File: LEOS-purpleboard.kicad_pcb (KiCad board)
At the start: 2 copper layers, 100 x 76.5 mm, 5 parts, among them J3 Conn_01x07_Socket, J4 Conn_01x07_Socket, J5 Conn_01x06_Socket, J6 Conn_01x06_Socket, J7 Conn_01x04_Pin

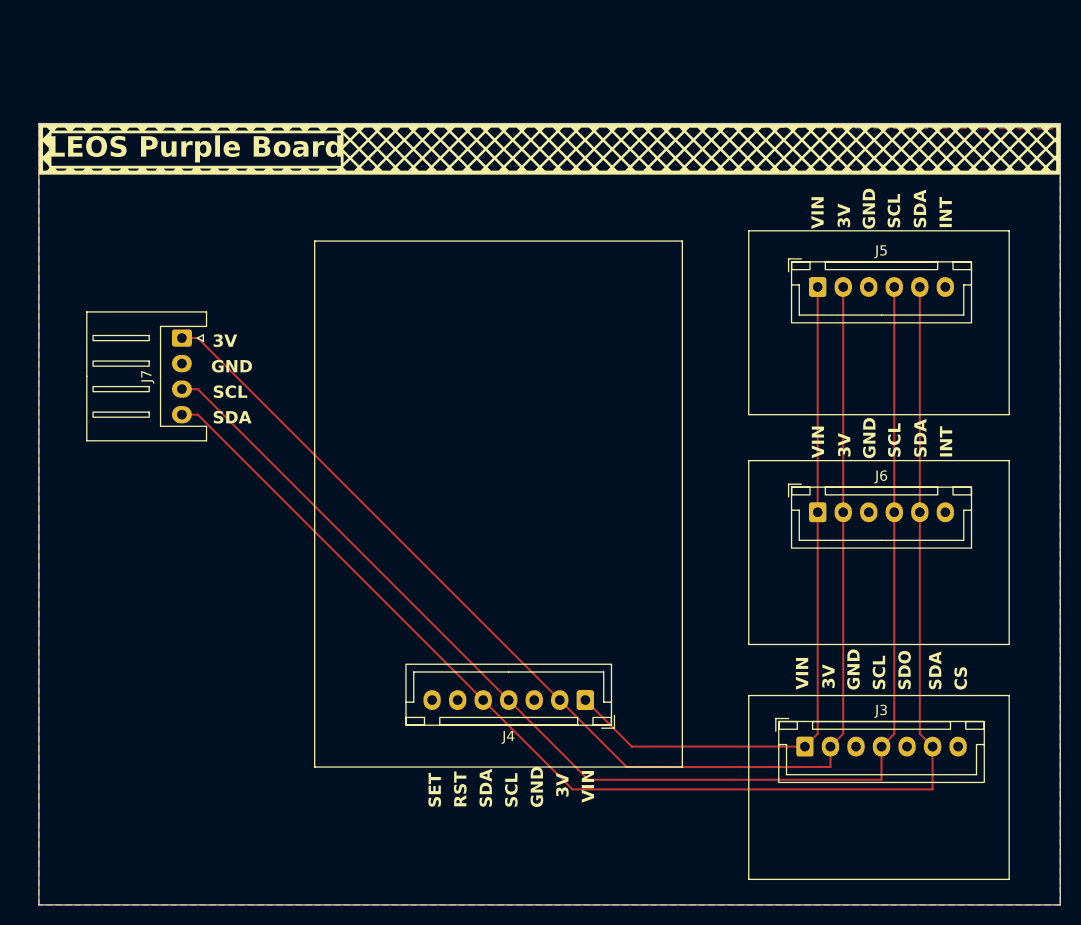
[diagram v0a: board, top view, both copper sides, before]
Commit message: Fix flipped pinouts, update 3D model, and redesign schematic
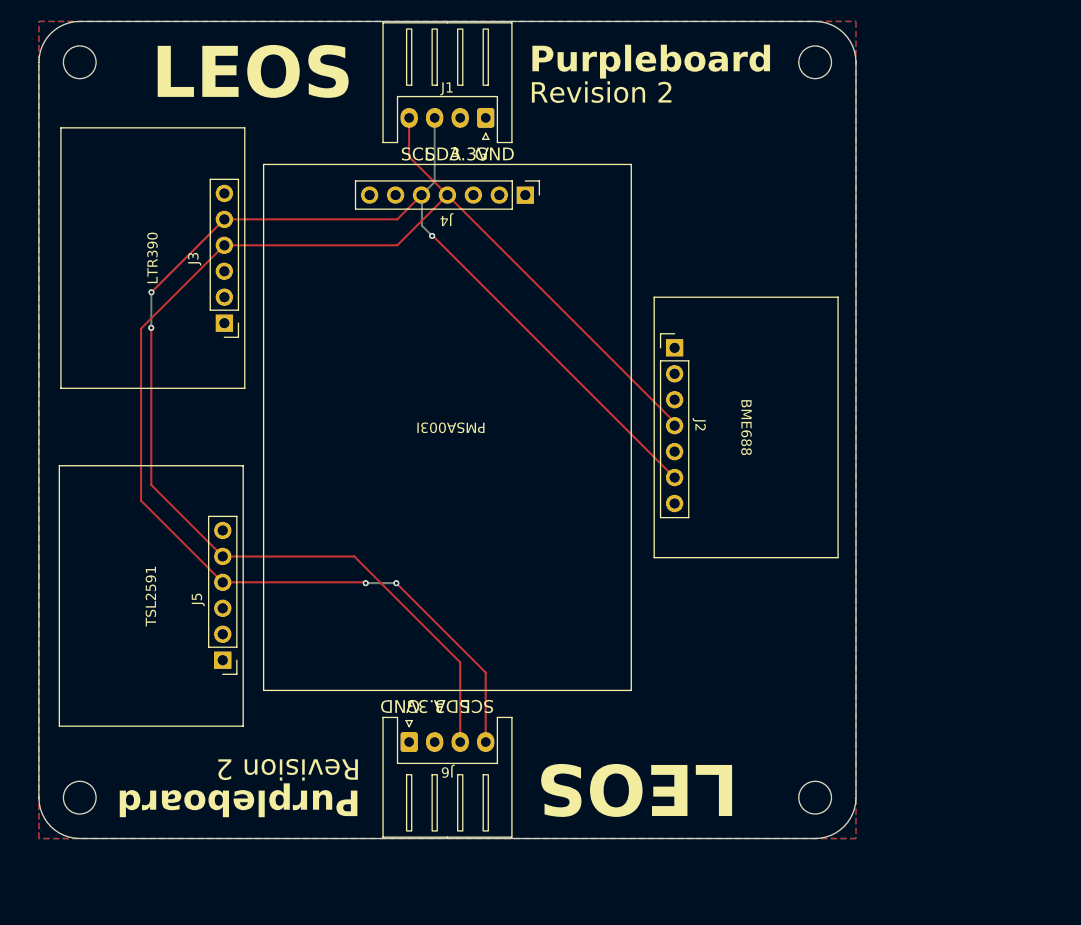
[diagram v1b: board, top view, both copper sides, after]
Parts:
- removed J7: Conn_01x04_Pin, Connector_JST:JST_XH_S4B-XH-A_1x04_P2.50mm_Horizontal
- added H1: MountingHole, MountingHole:MountingHole_3.2mm_M3, F.Cu at (104.0, 44.0)
- added H2: MountingHole, MountingHole:MountingHole_3.2mm_M3, F.Cu at (176.0, 44.0)
- added H3: MountingHole, MountingHole:MountingHole_3.2mm_M3, F.Cu at (104.0, 116.0)
- added H4: MountingHole, MountingHole:MountingHole_3.2mm_M3, F.Cu at (176.0, 116.0)
- added J1: JST XH, Connector_JST:JST_XH_S4B-XH-A_1x04_P2.50mm_Horizontal, F.Cu at (143.8, 49.4)
- added J2: BME688, Connector_PinHeader_2.54mm:PinHeader_1x07_P2.54mm_Vertical, F.Cu at (162.2, 72.0)
- J3: value Conn_01x07_Socket -> LTR390; footprint Connector_JST:JST_XH_B7B-XH-A_1x07_P2.50mm_Vertical -> Connector_PinHeader_2.54mm:PinHeader_1x06_P2.54mm_Vertical
- J4: value Conn_01x07_Socket -> PMSA003I; footprint Connector_JST:JST_XH_B7B-XH-A_1x07_P2.50mm_Vertical -> Connector_PinHeader_2.54mm:PinHeader_1x07_P2.54mm_Vertical
- J5: value Conn_01x06_Socket -> TSL2591; footprint Connector_JST:JST_XH_B6B-XH-A_1x06_P2.50mm_Vertical -> Connector_PinHeader_2.54mm:PinHeader_1x06_P2.54mm_Vertical
- J6: value Conn_01x06_Socket -> JST XH; footprint Connector_JST:JST_XH_B6B-XH-A_1x06_P2.50mm_Vertical -> Connector_JST:JST_XH_S4B-XH-A_1x04_P2.50mm_Horizontal
- moved J3 70.4 mm to (118.2, 69.5), turned to 180 degrees
- moved J5 68.8 mm to (118.0, 102.5), turned to 180 degrees
- moved J4 49.8 mm to (147.6, 57.0), turned to -90 degrees
- moved J6 45.9 mm to (136.2, 110.6)
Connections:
- net Net-(J3-Pin_4) renamed SCL
- J3 pad 1: Net-(J3-Pin_1) -> +3.3V
- J3 pad 2: +3.3V -> unconnected-(J3-Pin_2-Pad2)
- J3 pad 5: GND -> SDA
- J3 pad 6: Net-(J3-Pin_6) -> unconnected-(J3-Pin_6-Pad6)
- J4 pad 1: Net-(J3-Pin_1) -> +3.3V
- J4 pad 2: +3.3V -> unconnected-(J4-Pin_2-Pad2)
- J4 pad 5: Net-(J3-Pin_6) -> SDA
- J4 pad 7: GND -> unconnected-(J4-Pin_7-Pad7)
- J5 pad 1: Net-(J3-Pin_1) -> +3.3V
- J5 pad 2: +3.3V -> unconnected-(J5-Pin_2-Pad2)
- J5 pad 5: Net-(J3-Pin_6) -> SDA
- J5 pad 6: GND -> unconnected-(J5-Pin_6-Pad6)
- J6 pad 1: Net-(J3-Pin_1) -> GND
- J6 pad 3: GND -> SDA
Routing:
- net SDA: track 0.00 -> 140.6 mm, vias 0 -> 3
- net Net-(J3-Pin_6): track 138.4 -> 0.00 mm
- net +3.3V: track 128.4 -> 0.00 mm
- net Net-(J3-Pin_1): track 68.9 -> 0.00 mm
- net SCL: track 133.1 -> 140.7 mm, vias 0 -> 2
- added copper zone on F.Cu, net +3.3V
- removed copper zone on F.Cu, net GND
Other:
- board size 100 x 76.5 mm -> 80 x 80 mm
- board text added: "3.3V"
- board text added: "LEOS"
- board text added: "Purpleboard"
- board text added: "Revision 2"
- board text added: "SCK"
- board text added: "SDI"
- board text removed: "BACK"
- board text removed: "FRONT"
- board text removed: "LEFT"
- board text removed: "LEOS Purple Board"
- board text removed: "RIGHT"

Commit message: Add production date to board.
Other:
- board text added: "02/17/2026"
- board text added: "Revision 2.1"
- board text removed: "Revision 2"
